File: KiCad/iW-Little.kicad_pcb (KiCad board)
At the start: 4 copper layers, 21.5 x 35 mm, 28 parts, among them J1 USB_C_Receptacle_USB2.0, J3 Conn_01x10, J4 Conn_01x08, J5 Conn_02x02_Odd_Even, SW1 SW_Push, SW2 SW_Push, U1 STM32F030F4Px, U2 CH343P, U3 USBLC6-2P6, U4 AP2112K-3.3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

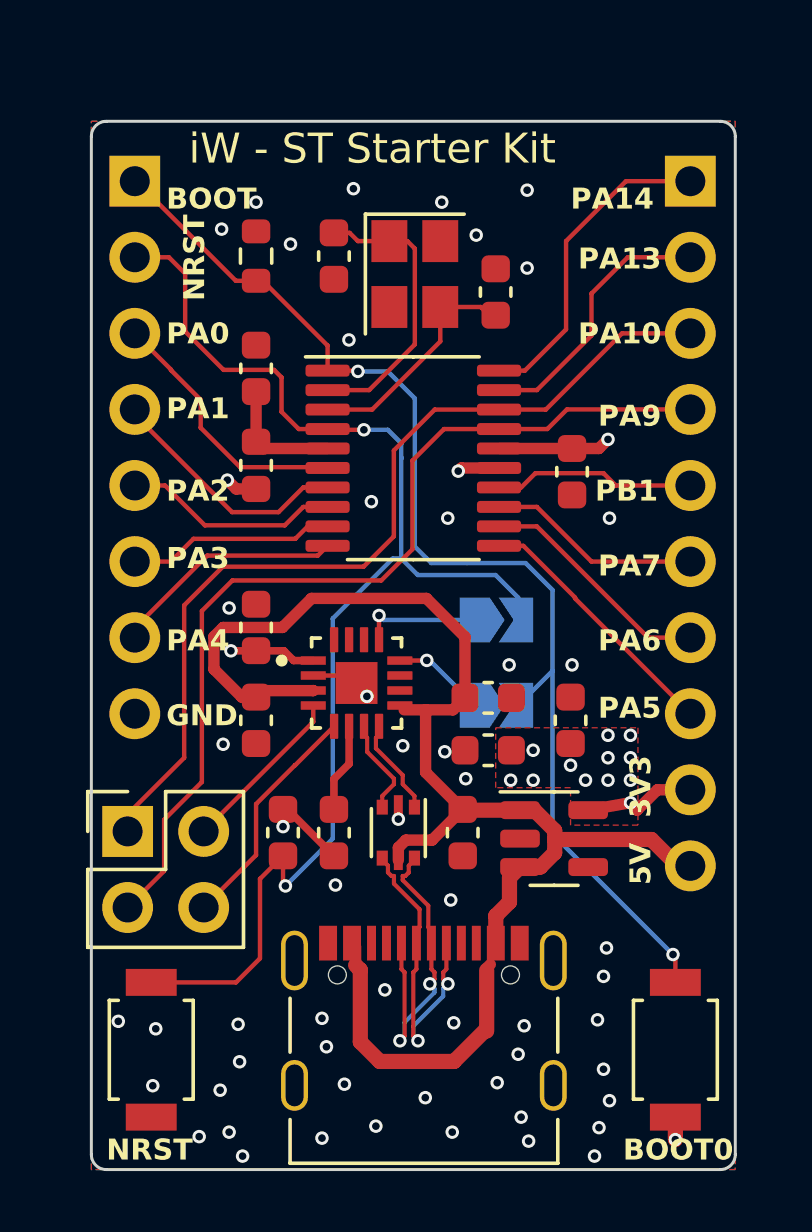
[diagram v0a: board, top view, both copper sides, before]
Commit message: size changed
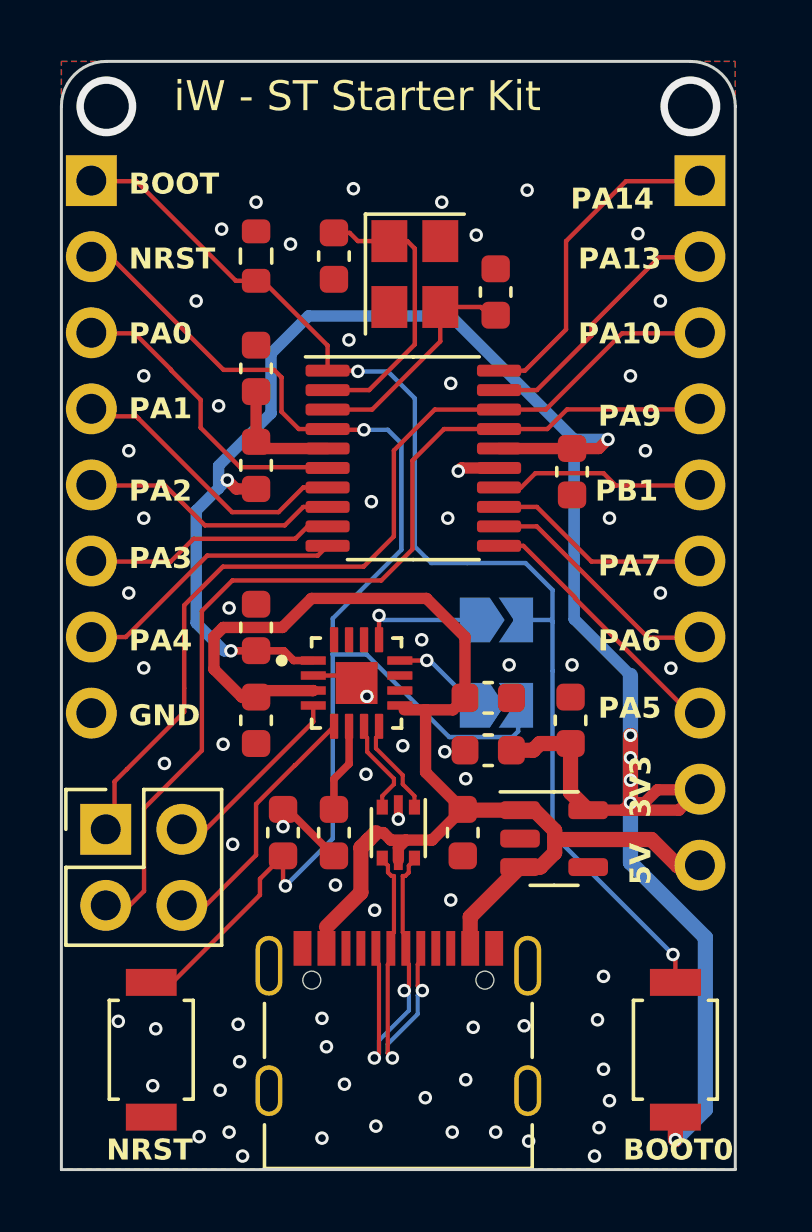
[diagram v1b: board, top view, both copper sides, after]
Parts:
- moved G*** 4.10 mm to (138.8, 75.5)
- moved J4 1.45 mm to (131.0, 67.0)
- moved J1 0.87 mm to (141.2, 95.1)
- moved J5 0.73 mm to (131.5, 88.6)
- moved J3 0.32 mm to (151.3, 67.0)
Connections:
- JP1 pad 2: BOOT0 -> NRST
- JP2 pad 2: NRST -> BOOT0
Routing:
- net +3.3V: track 12.3 -> 73.0 mm, vias 16 -> 8
- net +5V: track 49.1 -> 44.9 mm
- net NRST: track 43.8 -> 45.7 mm
- net PA2: track 7.19 -> 8.64 mm
- net PA0: track 8.86 -> 10.3 mm
- net PA4: track 7.87 -> 9.22 mm
- net PA1: track 8.28 -> 9.63 mm
- net BOOT0: track 39.4 -> 40.4 mm
- net PA3: track 7.49 -> 8.32 mm
- net USART1_RX: track 30.7 -> 31.4 mm
- net /USB_P: track 10.7 -> 11.3 mm
- net PA13: track 9.04 -> 8.43 mm
- net GND: vias 55 -> 70
- net (no net): vias 0 -> 2
- removed copper zone on F.Cu, net +3.3V
- removed copper zone on In2.Cu, net +3.3V
- removed copper zone on In1.Cu, net GND
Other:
- board size 21.5 x 35 mm -> 22.5 x 37 mm
- copper layers 4 -> 11
- board text added: "Jesus is the Son of God."
- board text added: "John 3.16"
